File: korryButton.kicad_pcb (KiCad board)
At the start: 2 copper layers, 30 x 30 mm, 15 parts, among them CN1 B2B-XH-A (LF)(SN), CN2 B2B-XH-A (LF)(SN), U1 SN74AHCT125DR, U2 B3B-XH-A(LF)(SN), U3 WS2811C, U4 WS2811C

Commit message: update
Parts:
- removed KEY1: ，12×12x7.3，:2.55N，:0.3mm, lcsc_footprints:C84931_KEY-TH_4P-L12_0-W12_0-P5_00-LS13_4-EH
- added SW1: 5.8 ZSGT, lcsc_footprints:C2681587_SW-TH_5_8ZSGT, F.Cu at (100.0, 126.2)
- U1: moved to F.Cu
- moved R3 1.52 mm to (95.2, 125.0)
- moved R2 1.27 mm to (95.5, 127.2)
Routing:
- net GND: track 83.1 -> 0.00 mm, vias 2 -> 0
- net VCC: track 60.6 -> 0.00 mm, vias 2 -> 0
- net Net-(U4-DO): track 21.9 -> 0.00 mm, vias 1 -> 0
- net Net-(U3-DO): track 21.1 -> 0.00 mm, vias 2 -> 0
- net Net-(R2-Pad1): track 17.8 -> 0.00 mm
- net Net-(U1-1Y): track 14.5 -> 0.00 mm, vias 1 -> 0
- net Net-(U1-1A): track 31.6 -> 22.3 mm
- net Net-(C1-Pad1): track 4.62 -> 0.67 mm
- net Net-(R2-Pad2): track 2.25 -> 0.00 mm
- added copper zone on B.Cu, net GND

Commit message: update
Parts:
- moved C1 10.8 mm to (95.2, 126.5)
- moved R1 8.78 mm to (95.2, 124.5)
- moved R2 7.50 mm to (99.2, 120.8), turned to 0 degrees
- moved R3 7.21 mm to (99.2, 119.0), turned to 180 degrees
- moved C2 3.46 mm to (93.3, 130.0)
- moved U1 3.26 mm to (100.0, 132.6)
- moved CN1 2.00 mm to (111.0, 113.0), turned to 180 degrees
- moved CN2 2.00 mm to (89.0, 113.0), turned to 180 degrees
- moved U2 2.00 mm to (100.0, 113.0), turned to 0 degrees
- moved SW1 1.25 mm to (100.0, 125.0)
- moved LED1 0.63 mm to (110.0, 125.0)
- moved LED2 0.63 mm to (90.0, 125.0)
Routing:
- net VCC: track 0.00 -> 45.6 mm, vias 0 -> 4
- net Net-(U4-DO): track 0.00 -> 24.7 mm
- net Net-(U3-DO): track 0.00 -> 21.9 mm
- net Net-(U1-1Y): track 0.00 -> 15.4 mm
- net Net-(R2-Pad1): track 0.00 -> 8.46 mm, vias 0 -> 1
- net GND: track 0.00 -> 4.49 mm, vias 0 -> 3
- net Net-(C1-Pad1): track 0.67 -> 4.75 mm
- net Net-(U1-1A): track 22.3 -> 20.0 mm
- net Net-(R2-Pad2): track 0.00 -> 2.00 mm
- net Net-(LED1-R): track 8.95 -> 10.4 mm
- net Net-(LED2-B): track 8.02 -> 8.65 mm
- net Net-(LED1-B): track 8.02 -> 8.65 mm
- net Net-(LED2-R): track 8.95 -> 9.58 mm

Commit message: update pcb
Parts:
- CN1, CN2, U2: moved to B.Cu
- R2, R3: moved to F.Cu
- moved R3 5.95 mm to (104.6, 121.6)
- moved CN2 5.20 mm to (89.0, 118.2), turned to 0 degrees
- moved U2 5.20 mm to (100.0, 118.2), turned to 180 degrees
- moved CN1 4.00 mm to (111.0, 117.0), turned to 0 degrees
- moved C3 3.97 mm to (112.7, 126.8), turned to -90 degrees
- moved C1 3.71 mm to (95.0, 122.8)
- moved C2 2.67 mm to (94.2, 127.5)
- moved U3 2.50 mm to (110.0, 131.0)
- moved U4 2.50 mm to (90.0, 131.0)
- moved R2 1.50 mm to (100.8, 120.8), turned to 180 degrees
- moved R1 0.39 mm to (95.0, 124.8)
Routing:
- net VCC: track 45.6 -> 58.0 mm
- net Net-(U4-DO): track 24.7 -> 15.8 mm
- net Net-(R2-Pad1): track 8.46 -> 2.96 mm, vias 1 -> 0
- net GND: track 4.49 -> 7.91 mm, vias 3 -> 5
- net Net-(LED1-R): track 10.4 -> 7.08 mm
- net Net-(U1-1A): track 20.0 -> 17.0 mm
- net Net-(LED1-G): track 8.64 -> 6.14 mm
- net Net-(LED2-R): track 9.58 -> 7.08 mm
- net Net-(LED2-B): track 8.65 -> 6.15 mm
- net Net-(LED1-B): track 8.65 -> 6.15 mm
- net Net-(U1-1Y): track 15.4 -> 12.9 mm, vias 0 -> 2
- net Net-(LED2-G): track 8.53 -> 6.14 mm
- net Net-(R2-Pad2): track 2.00 -> 0.00 mm
- net Net-(U3-DO): track 21.9 -> 21.2 mm

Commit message: Update korryButton.kicad_pcb
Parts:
- C2: moved to F.Cu
- U1: moved to B.Cu
- moved CN2 17.8 mm to (89.8, 136.0)
- moved U3 12.0 mm to (110.0, 119.0)
- moved CN1 3.09 mm to (110.2, 114.0), turned to 180 degrees
- turned U1 to 0 degrees
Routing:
- net Net-(U1-1A): track 17.0 -> 0.00 mm
- net Net-(U4-DO): track 15.8 -> 3.80 mm
- net VCC: track 58.0 -> 48.1 mm, vias 4 -> 2
- net Net-(U1-1Y): track 12.9 -> 19.9 mm, vias 2 -> 1
- net GND: track 7.91 -> 1.87 mm, vias 5 -> 2
- net Net-(U3-DO): track 21.2 -> 27.2 mm
- net Net-(LED1-G): track 6.14 -> 8.66 mm
- net Net-(LED1-B): track 6.15 -> 8.49 mm
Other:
- outline, holes or cut-outs redrawn

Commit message: update schematic, pcb
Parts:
- removed CN2: B2B-XH-A (LF)(SN), lcsc_footprints:C158012_CONN-TH_B2B-XH-A-LF-SN
- removed U2: B3B-XH-A(LF)(SN), lcsc_footprints:C144394_CONN-TH_3P-P2_50_A2501WV2-3P
- added C4: 100nF (104) ±10% 50V, lcsc_footprints:C1591_C0603, F.Cu at (95.7, 127.2)
- C2, R3: moved to B.Cu
- CN1: value B2B-XH-A (LF)(SN) -> B5B-XH-A (LF)(SN); footprint lcsc_footprints:C158012_CONN-TH_B2B-XH-A-LF-SN -> lcsc_footprints:C157991_CONN-TH_B5B-XH-A-LF-SN
- U1: moved to F.Cu
- moved C3 19.5 mm to (93.2, 127.5), turned to 180 degrees
- moved C2 18.7 mm to (110.0, 117.5), turned to 0 degrees
- moved CN1 10.3 mm to (99.9, 114.0)
- moved R2 6.52 mm to (105.0, 125.7)
- moved R3 2.33 mm to (105.0, 123.9)
- moved R1 2.00 mm to (95.0, 122.8)
- moved C1 1.80 mm to (95.0, 121.0)
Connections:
- CN1 pad 1: Net-(U1-1A) -> VCC
- R2 pad 1: Net-(R2-Pad1) -> Net-(CN1-Pad5)
- R3 pad 2: Net-(R2-Pad1) -> Net-(CN1-Pad5)
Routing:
- net Net-(U1-1A): track 0.00 -> 25.8 mm, vias 0 -> 2
- net VCC: track 48.1 -> 72.7 mm, vias 2 -> 4
- net Net-(U4-DO): track 3.80 -> 23.5 mm
- net Net-(CN1-Pad5): track 0.00 -> 13.3 mm, vias 0 -> 2
- net GND: track 1.87 -> 15.1 mm, vias 2 -> 4
- net Net-(U1-1Y): track 19.9 -> 26.7 mm, vias 1 -> 0
- net Net-(R2-Pad2): track 0.00 -> 5.47 mm
- net Net-(R2-Pad1): track 2.96 -> 0.00 mm

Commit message: update pcb
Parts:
- moved U4 0.73 mm to (90.0, 131.7)
- turned R3 to 0 degrees
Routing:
- net VCC: track 72.7 -> 82.3 mm
- net Net-(LED2-R): track 7.08 -> 7.81 mm
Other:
- board text added: "5V"
- board text added: "DI"
- board text added: "DO"
- board text added: "G"
- board text added: "SW"

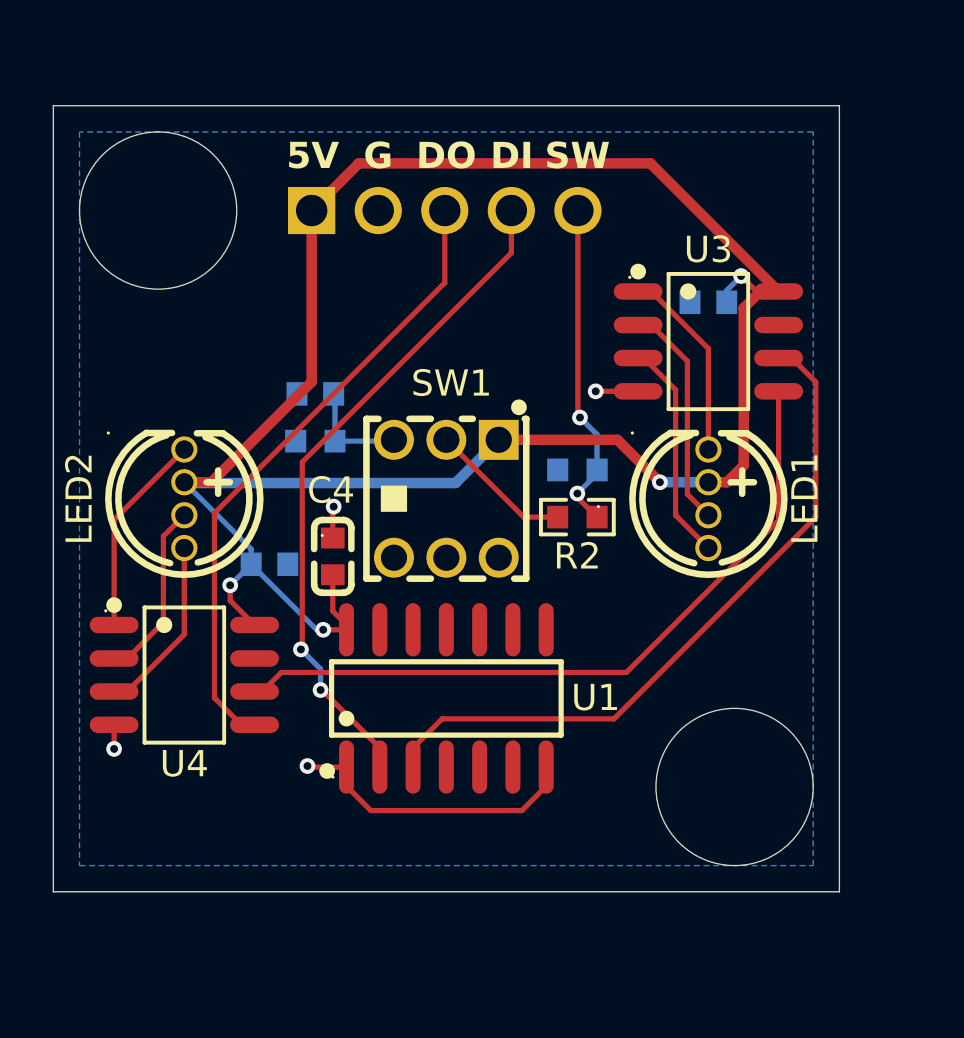
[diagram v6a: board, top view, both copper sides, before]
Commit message: update C1 position, pcb layout
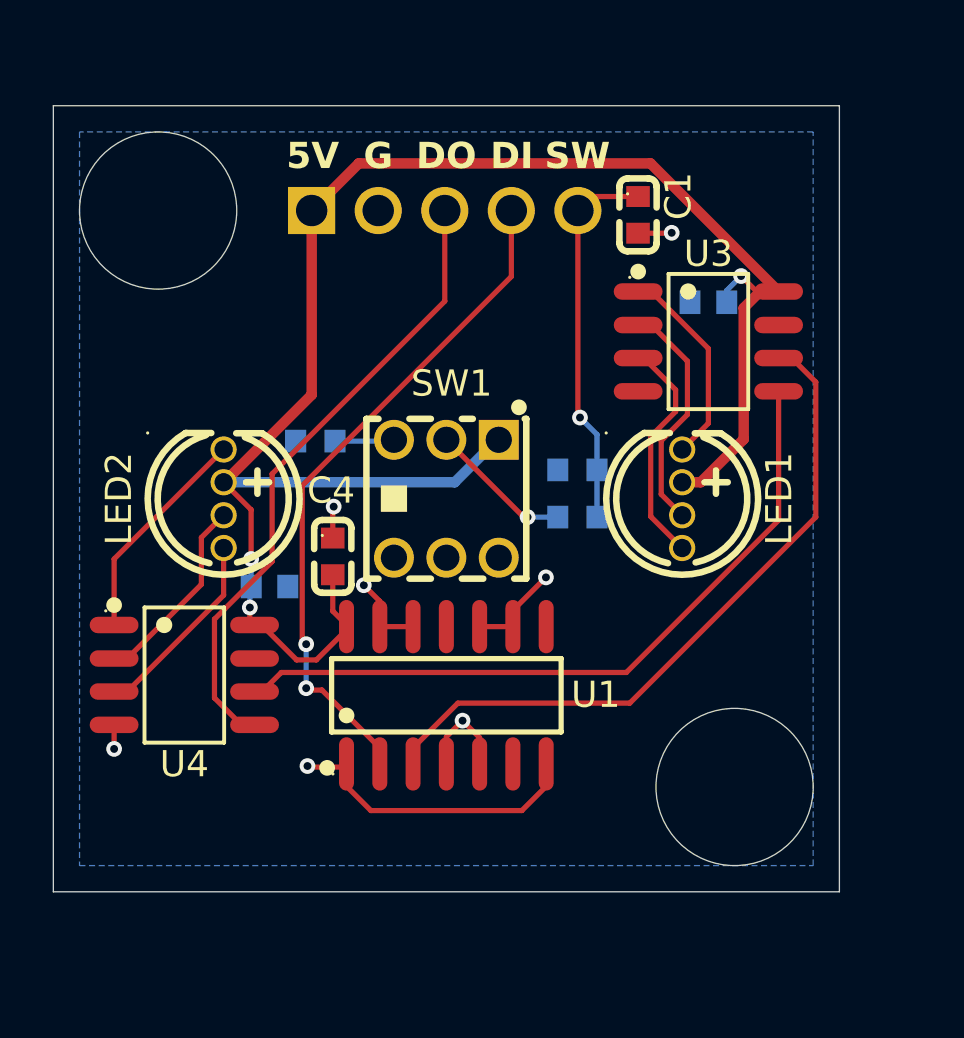
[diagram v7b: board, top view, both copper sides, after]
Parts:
- C1: moved to F.Cu
- R2: moved to B.Cu
- moved C1 14.1 mm to (107.3, 114.2), turned to -90 degrees
- moved LED2 1.50 mm to (91.5, 125.0)
- moved LED1 1.00 mm to (109.0, 125.0)
- moved C3 0.85 mm to (93.2, 128.3)
- moved U1 0.12 mm to (100.0, 132.5)
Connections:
- CN1 pad 5: Net-(CN1-Pad5) -> Net-(C1-Pad1)
- R1 pad 1: Net-(C1-Pad1) -> Net-(R1-Pad1)
- R2 pad 1: Net-(CN1-Pad5) -> Net-(C1-Pad1)
- R3 pad 2: Net-(CN1-Pad5) -> Net-(C1-Pad1)
- SW1 pad 3: Net-(C1-Pad1) -> Net-(R1-Pad1)
- U1 pad 10: unconnected-(U1-3OE#-Pad10) -> GND
- U1 pad 12: unconnected-(U1-4A-Pad12) -> GND
- U1 pad 13: unconnected-(U1-4OE#-Pad13) -> GND
- U1 pad 4: unconnected-(U1-2OE#-Pad4) -> GND
- U1 pad 5: unconnected-(U1-2A-Pad5) -> GND
- U1 pad 9: unconnected-(U1-3A-Pad9) -> GND
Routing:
- net Net-(CN1-Pad5): track 13.2 -> 0.00 mm, vias 2 -> 0
- net VCC: track 82.3 -> 69.7 mm, vias 4 -> 3
- net Net-(C1-Pad1): track 4.09 -> 15.1 mm, vias 0 -> 1
- net GND: track 15.1 -> 25.4 mm, vias 4 -> 7
- net Net-(R1-Pad1): track 0.00 -> 2.27 mm
- net Net-(LED2-G): track 6.37 -> 7.49 mm
- net Net-(LED2-B): track 6.38 -> 7.50 mm
- net Net-(LED2-R): track 7.81 -> 8.43 mm
- net Net-(R2-Pad2): vias 0 -> 1

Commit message: udpate leds to be DNP
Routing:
- net GND: track 25.4 -> 27.0 mm, vias 7 -> 8
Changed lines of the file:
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@@
 			)
 		)
-		(attr through_hole)
+		(attr through_hole exclude_from_pos_files exclude_from_bom dnp)
 		(duplicate_pad_numbers_are_jumpers no)
 		(fp_line
@@
 			)
 		)
-		(attr through_hole)
+		(attr through_hole exclude_from_pos_files exclude_from_bom dnp)
 		(duplicate_pad_numbers_are_jumpers no)
 		(fp_line
@@
 				(font
 					(size 1.27 1.27)
+					(thickness 0.15)
 				)
 			)
@@
 			(net "unconnected-(U1-2Y-Pad6)")
 			(pinfunction "2Y_6")
-			(pintype "unspecified")
+			(pintype "unspecified+no_connect")
 		)
 		(pad "7" smd oval
@@
 			(net "unconnected-(U1-3Y-Pad8)")
 			(pinfunction "3Y_8")
-			(pintype "unspecified")
+			(pintype "unspecified+no_connect")
 		)
 		(pad "9" smd oval
@@
 			(net "unconnected-(U1-4Y-Pad11)")
 			(pinfunction "4Y_11")
-			(pintype "unspecified")
+			(pintype "unspecified+no_connect")
 		)
 		(pad "12" smd oval
@@
 			(net "unconnected-(U4-NC-Pad7)")
 			(pinfunction "NC_7")
-			(pintype "unspecified")
+			(pintype "unspecified+no_connect")
 		)
 		(pad "8" smd oval
@@
 			(net "unconnected-(U3-NC-Pad7)")
 			(pinfunction "NC_7")
-			(pintype "unspecified")
+			(pintype "unspecified+no_connect")
 		)
 		(pad "8" smd oval
@@
 			(net "unconnected-(SW1-Pad4)")
 			(pinfunction "4_4")
-			(pintype "unspecified")
+			(pintype "unspecified+no_connect")
 		)
 		(pad "5" thru_hole circle
@@
 			(net "unconnected-(SW1-Pad5)")
 			(pinfunction "5_5")
-			(pintype "unspecified")
+			(pintype "unspecified+no_connect")
 		)
 		(pad "6" thru_hole circle
@@
 			(net "unconnected-(SW1-Pad6)")
 			(pinfunction "6_6")
-			(pintype "unspecified")
+			(pintype "unspecified+no_connect")
 		)
 		(embedded_fonts no)
@@
 			(net "GND")
 			(pinfunction "1_1")
-			(pintype "input")
+			(pintype "passive")
 		)
 		(pad "2" smd rect
@@
 			(net "Net-(C1-Pad1)")
 			(pinfunction "2_2")
-			(pintype "input")
+			(pintype "passive")
 		)
 		(embedded_fonts no)
@@
 			(net "Net-(C1-Pad1)")
 			(pinfunction "1_1")
-			(pintype "input")
+			(pintype "passive")
 		)
 		(pad "2" smd rect
@@
 			(net "Net-(R2-Pad2)")
 			(pinfunction "2_2")
-			(pintype "input")
+			(pintype "passive")
 		)
 		(embedded_fonts no)
@@
 			(net "Net-(R1-Pad1)")
 			(pinfunction "1_1")
-			(pintype "input")
+			(pintype "passive")
 		)
 		(pad "2" smd rect
@@
 			(net "GND")
 			(pinfunction "2_2")
-			(pintype "input")
+			(pintype "passive")
 		)
 		(embedded_fonts no)
@@
 	)
 	(segment
-		(start 102.95 125.7)
-		(end 100 122.75)
-		(width 0.2)
-		(layer "F.Cu")
-		(net "Net-(R2-Pad2)")
-	)
-	(segment
-		(start 103.1 125.7)
-		(end 102.95 125.7)
-		(width 0.2)
-		(layer "F.Cu")
-		(net "Net-(R2-Pad2)")
-	)
-	(via
-		(at 103.1 125.7)
-		(size 0.6)
-		(drill 0.3)
-		(layers "F.Cu" "B.Cu")
-		(net "Net-(R2-Pad2)")
-	)
-	(segment
-		(start 104.25 125.7)
-		(end 103.1 125.7)
-		(width 0.2)
-		(layer "B.Cu")
-		(net "Net-(R2-Pad2)")
-	)
-	(segment
 		(start 87.32 127.3)
 		(end 87.32 129.8175)
@@
 	)
 	(segment
+		(start 105.02 121.82)
+		(end 105.02 114)
+		(width 0.2)
+		(layer "F.Cu")
+		(net "Net-(C1-Pad1)")
+	)
+	(segment
+		(start 107.315 113.465)
+		(end 105.555 113.465)
+		(width 0.2)
+		(layer "F.Cu")
+		(net "Net-(C1-Pad1)")
+	)
+	(segment
+		(start 105.555 113.465)
+		(end 105.02 114)
+		(width 0.2)
+		(layer "F.Cu")
+		(net "Net-(C1-Pad1)")
+	)
+	(segment
+		(start 105.1 121.9)
+		(end 105.02 121.82)
+		(width 0.2)
+		(layer "F.Cu")
+		(net "Net-(C1-Pad1)")
+	)
+	(via
+		(at 105.1 121.9)
+		(size 0.6)
+		(drill 0.3)
+		(layers "F.Cu" "B.Cu")
+		(net "Net-(C1-Pad1)")
+	)
+	(segment
+		(start 105.75 123.9)
+		(end 105.75 122.55)
+		(width 0.2)
+		(layer "B.Cu")
+		(net "Net-(C1-Pad1)")
+	)
+	(segment
+		(start 104.65 114.37)
+		(end 105.02 114)
+		(width 0.2)
+		(layer "B.Cu")
+		(net "Net-(C1-Pad1)")
+	)
+	(segment
+		(start 105.75 123.9)
+		(end 105.75 125.7)
+		(width 0.2)
+		(layer "B.Cu")
+		(net "Net-(C1-Pad1)")
+	)
+	(segment
+		(start 105.75 122.55)
+		(end 105.1 121.9)
+		(width 0.2)
+		(layer "B.Cu")
+		(net "Net-(C1-Pad1)")
+	)
+	(segment
+		(start 104.63 114.37)
+		(end 104.65 114.37)
+		(width 0.2)
+		(layer "B.Cu")
+		(net "Net-(C1-Pad1)")
+	)
+	(segment
+		(start 107.32 120.9)
+		(end 105.7 120.9)
+		(width 0.2)
+		(layer "F.Cu")
+		(net "GND")
+	)
+	(segment
 		(start 94.74 135.24)
 		(end 94.7 135.2)
@@
 	)
 	(via
+		(at 105.7 120.9)
+		(size 0.6)
+		(drill 0.3)
+		(layers "F.Cu" "B.Cu")
+		(net "GND")
+	)
+	(via
 		(at 95.7 125.3)
 		(size 0.6)
@@
 	)
 	(segment
-		(start 94.5 124.5)
-		(end 102.48 116.52)
+		(start 94.65 130.55)
+		(end 94.65 124.35)
 		(width 0.2)
 		(layer "F.Cu")
@@
 	)
 	(segment
-		(start 102.48 116.52)
-		(end 102.48 114)
+		(start 97.46 135.24)
+		(end 97.46 134.508)
 		(width 0.2)
 		(layer "F.Cu")
@@
 	)
 	(segment
-		(start 97.46 135.24)
-		(end 97.46 134.508)
+		(start 95.252 132.3)
+		(end 94.72 132.3)
 		(width 0.2)
 		(layer "F.Cu")
@@
 	)
 	(segment
-		(start 95.252 132.3)
-		(end 94.72 132.3)
+		(start 94.65 124.35)
+		(end 102.48 116.52)
 		(width 0.2)
 		(layer "F.Cu")
@@
 	)
 	(segment
-		(start 94.5 130.4)
-		(end 94.5 124.5)
+		(start 102.48 116.52)
+		(end 102.48 114)
 		(width 0.2)
 		(layer "F.Cu")
@@
 	)
 	(segment
-		(start 105.02 121.82)
-		(end 105.02 114)
-		(width 0.2)
-		(layer "F.Cu")
-		(net "Net-(C1-Pad1)")
-	)
-	(segment
-		(start 107.315 113.465)
-		(end 105.555 113.465)
-		(width 0.2)
-		(layer "F.Cu")
-		(net "Net-(C1-Pad1)")
-	)
-	(segment
-		(start 105.555 113.465)
-		(end 105.02 114)
+		(start 102.95 125.7)
+		(end 100 122.75)
 		(width 0.2)
 		(layer "F.Cu")
-		(net "Net-(C1-Pad1)")
+		(net "Net-(R2-Pad2)")
 	)
 	(segment
-		(start 105.1 121.9)
-		(end 105.02 121.82)
+		(start 103.1 125.7)
+		(end 102.95 125.7)
 		(width 0.2)
 		(layer "F.Cu")
-		(net "Net-(C1-Pad1)")
+		(net "Net-(R2-Pad2)")
 	)
 	(via
-		(at 105.1 121.9)
+		(at 103.1 125.7)
 		(size 0.6)
 		(drill 0.3)
 		(layers "F.Cu" "B.Cu")
-		(net "Net-(C1-Pad1)")
-	)
-	(segment
-		(start 105.75 123.9)
-		(end 105.75 122.55)
-		(width 0.2)
-		(layer "B.Cu")
-		(net "Net-(C1-Pad1)")
-	)
-	(segment
-		(start 104.65 114.37)
-		(end 105.02 114)
-		(width 0.2)
-		(layer "B.Cu")
-		(net "Net-(C1-Pad1)")
-	)
-	(segment
-		(start 105.75 123.9)
-		(end 105.75 125.7)
-		(width 0.2)
-		(layer "B.Cu")
-		(net "Net-(C1-Pad1)")
-	)
-	(segment
-		(start 105.75 122.55)
-		(end 105.1 121.9)
-		(width 0.2)
-		(layer "B.Cu")
-		(net "Net-(C1-Pad1)")
+		(net "Net-(R2-Pad2)")
 	)
 	(segment
-		(start 104.63 114.37)
-		(end 104.65 114.37)
+		(start 104.25 125.7)
+		(end 103.1 125.7)
 		(width 0.2)
 		(layer "B.Cu")
-		(net "Net-(C1-Pad1)")
+		(net "Net-(R2-Pad2)")
 	)
 	(segment
